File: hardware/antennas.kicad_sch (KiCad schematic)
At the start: 21 parts, among them J1001 132134

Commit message: Refine schematics
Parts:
- removed R1001, R1002, R1003, R1004, R1005, R1006, R1007, R1008: 0 Ω, perfect_footprints:R_0402_1005Metric, symbol Device:R
- added R79, R80, R81, R82, R83, R85, R86: 0 Ω, perfect_footprints:R_0402_1005Metric, symbol Device:R
- added R84: 0 Ω, perfect_footprints:R_0201_0603Metric, symbol Device:R
- renumbered AE1001 to AE1, C1001 to C52, C1002 to C53, C1003 to C54, C1004 to C55, C1005 to C56, D1001 to D15, J1001 to J20, L1001 to L3, L1002 to L4, L1003 to L5, L1004 to L6, L1005 to L7
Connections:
- net ANT: now also R79.1, R80.1
- net ANT_PCB_FILTERED: now also R82.1, R84.1
- net ANT_PCB_MATCHED: now also R84.2, R86.1
- net ANT_SEL_PCB: now also R80.2
- net ANT_SEL_SMA: now also R79.2, R81.1, R83.1
- net ANT_SMA_MATCHED: now also R83.2, R85.1
- net GND: now also R81.2, R82.2, R85.2, R86.2
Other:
- note added: "Antenna front-end"
- note added: "Antenna selection"
- note added: "Bandpass filter"
- note added: "Matching network"
- note added: "Notes"

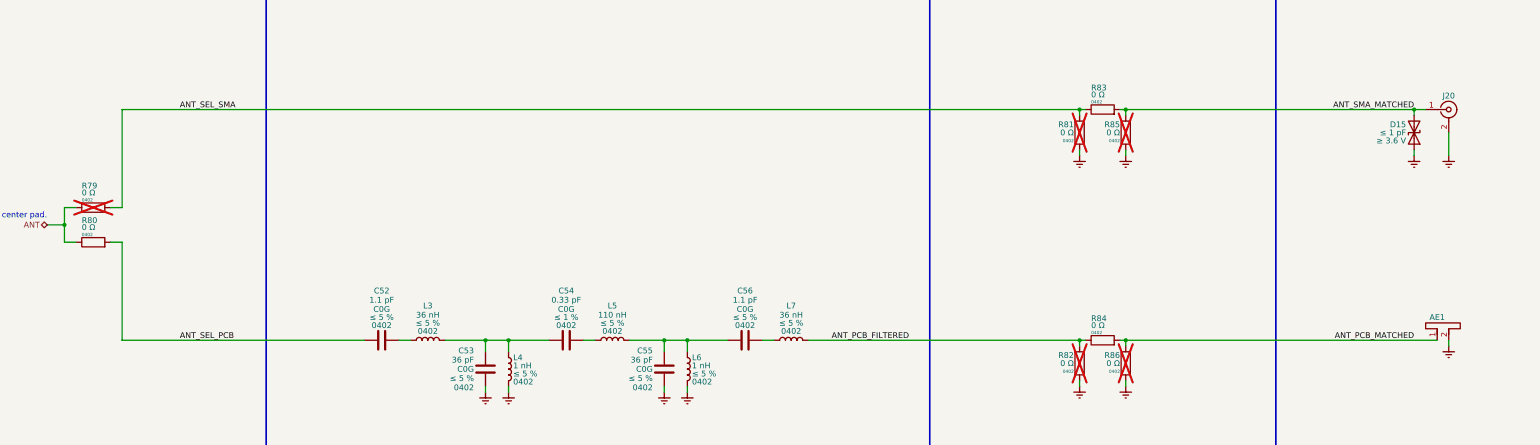
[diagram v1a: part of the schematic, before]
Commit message: HW: Redo MDM UART
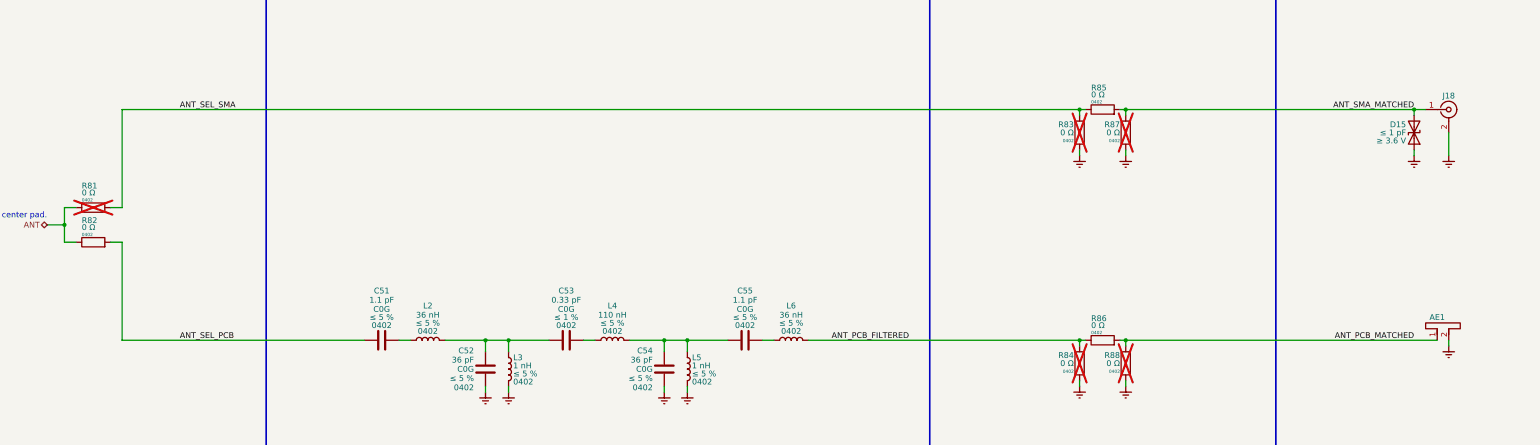
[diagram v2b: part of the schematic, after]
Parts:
- renumbered C52 to C51, C53 to C52, C54 to C53, C55 to C54, C56 to C55, J20 to J18, L3 to L2, L4 to L3, L5 to L4, L6 to L5, L7 to L6, R79 to R81, R80 to R82, R81 to R83, R82 to R84, R83 to R85, R84 to R86, R85 to R87, R86 to R88

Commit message: HW: BAT_DETn -> USB_DET
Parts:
- renumbered AE1 to AE701, C51 to C701, C52 to C702, C53 to C703, C54 to C704, C55 to C705, D15 to D701, J18 to J701, L2 to L701, L3 to L702, L4 to L703, L5 to L704, L6 to L705, R81 to R701, R82 to R702, R83 to R703, R84 to R704, R85 to R705, R86 to R706, R87 to R707, R88 to R708

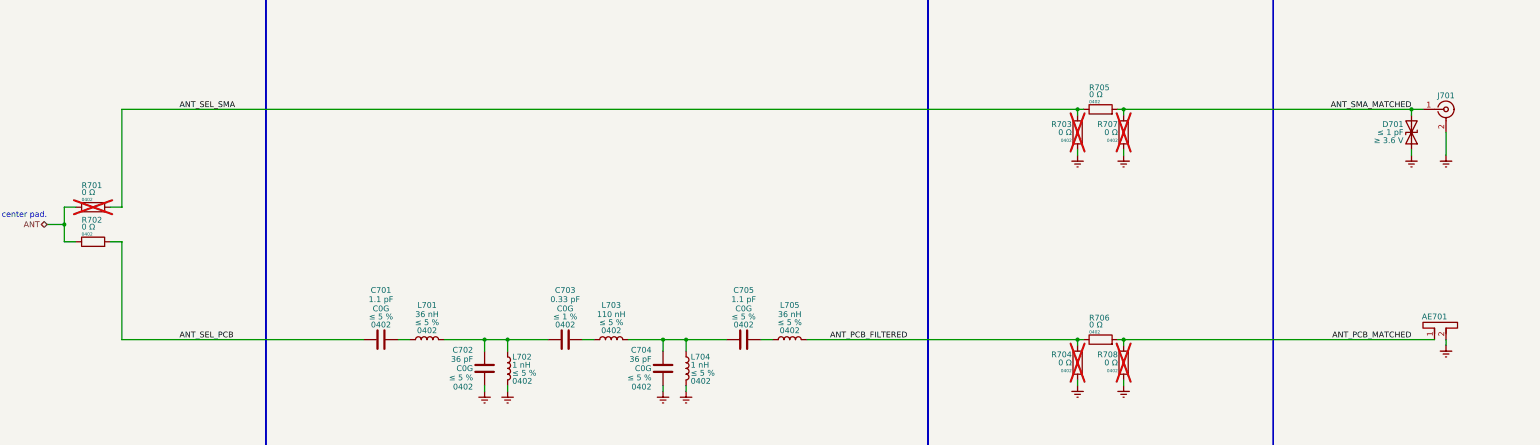
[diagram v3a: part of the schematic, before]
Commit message: HW: Move SIM to Modem
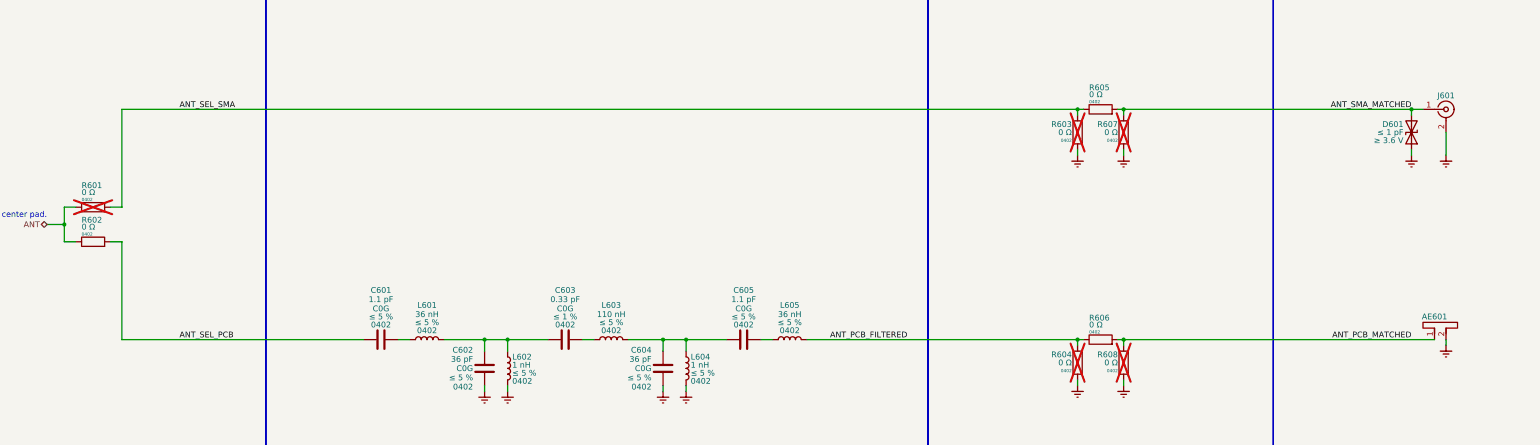
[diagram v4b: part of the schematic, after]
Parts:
- renumbered AE701 to AE601, C701 to C601, C702 to C602, C703 to C603, C704 to C604, C705 to C605, D701 to D601, J701 to J601, L701 to L601, L702 to L602, L703 to L603, L704 to L604, L705 to L605, R701 to R601, R702 to R602, R703 to R603, R704 to R604, R705 to R605, R706 to R606, R707 to R607, R708 to R608

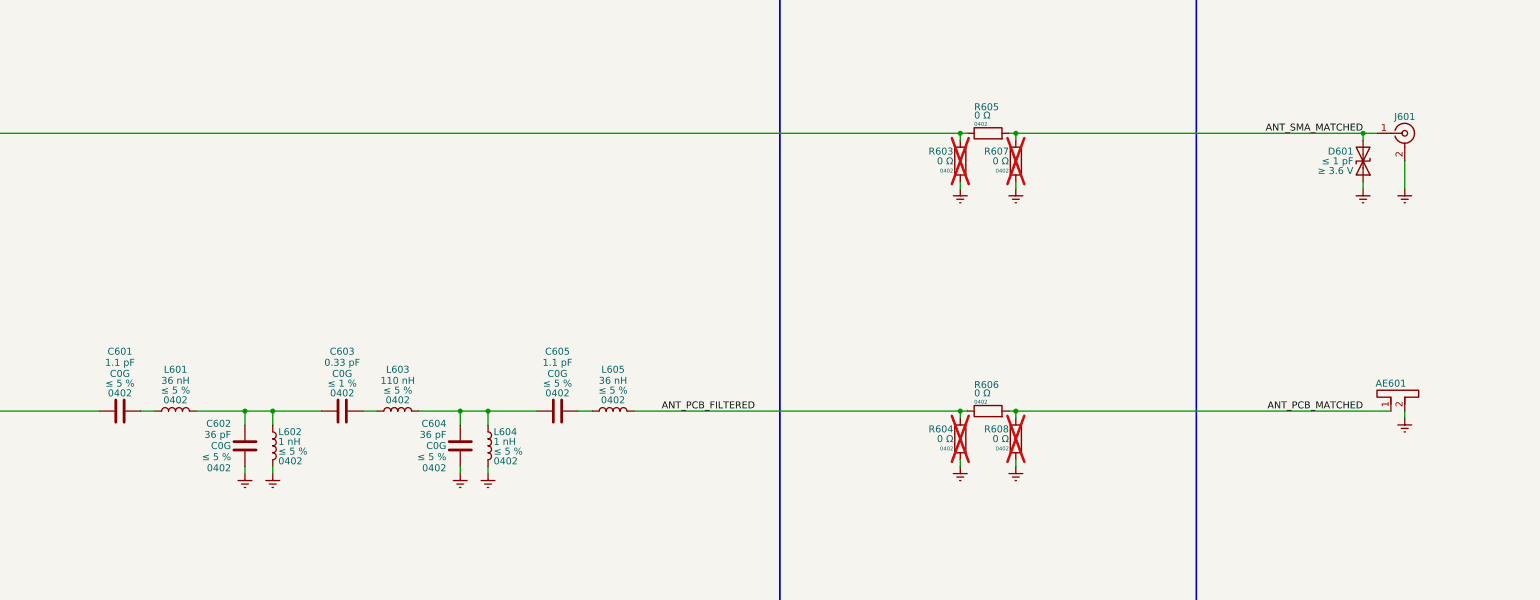
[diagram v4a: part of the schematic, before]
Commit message: HW: Refine Antennas
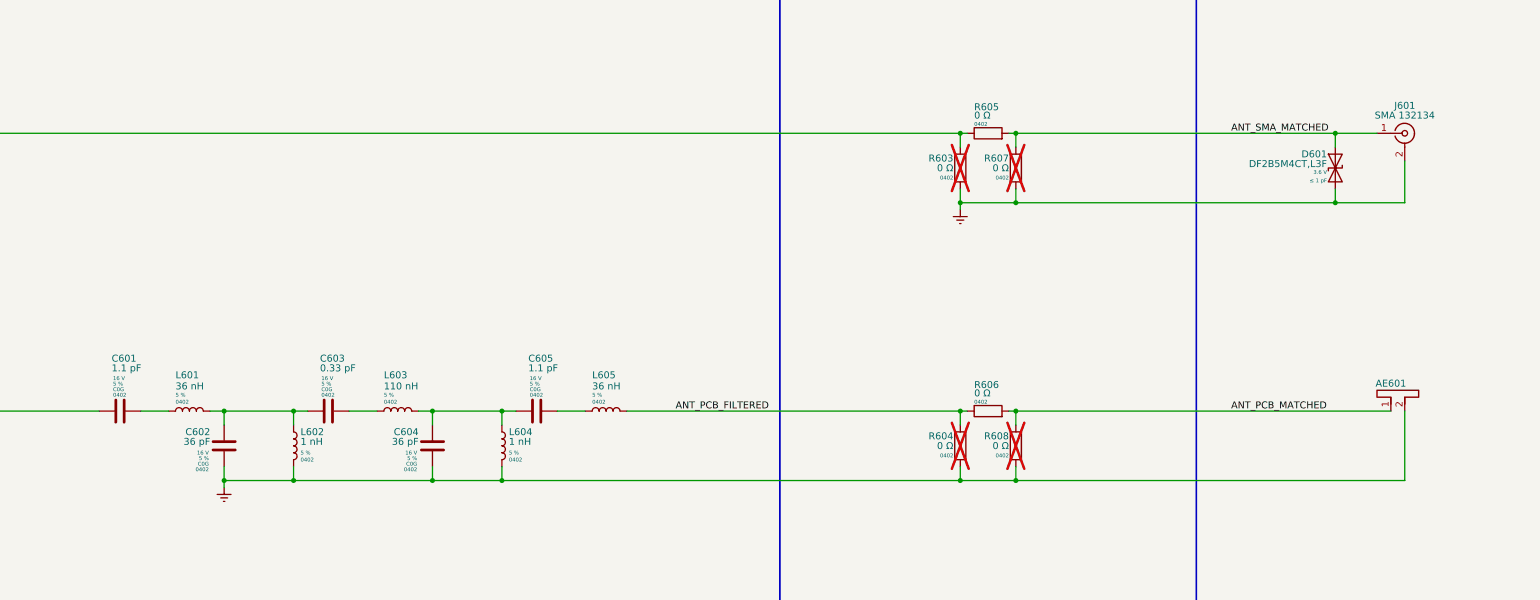
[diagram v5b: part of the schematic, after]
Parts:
- C601, C605: Class C0G -> (none); DigiKey Part Number 732-13231-1-ND -> (none); MPN 885392005006 -> (none); Manufacturer Würth Elektronik -> (none); Temperature coefficient (none) -> C0G; Tolerance ≤ 5 % -> 5 %; Voltage rating (none) -> 16 V
- C602, C604: footprint perfect_footprints:C_0402_1005Metric -> perfect_footprints:C_0201_0603Metric; Class C0G -> (none); DigiKey Part Number 490-GJM1555C1H360FB01DCT-ND -> (none); MPN GJM1555C1H360FB01D -> (none); Manufacturer Murata Electronics -> (none); Temperature coefficient (none) -> C0G; Tolerance ≤ 5 % -> 5 %; Voltage rating (none) -> 16 V
- C603: Class C0G -> (none); DigiKey Part Number 732-13226-1-ND -> (none); MPN 885392005001 -> (none); Manufacturer Würth Elektronik -> (none); Temperature coefficient (none) -> C0G; Tolerance ≤ 1 % -> 5 %; Voltage rating (none) -> 16 V
- D601: Breakdown voltage (none) -> 3.6 V; Digi-Key Part Number (none) -> DF2B5M4CTL3FCT-ND; DigiKey Part Number DF2B5M4CTL3FCT-ND -> (none); Footprint review check + -> (none); Voltage ≥ 3.6 V -> (none)
- J601: value 132134 -> SMA 132134
- L601, L605: DigiKey Part Number 732-7447650136CT-ND -> (none); MPN 7447650136 -> (none); Manufacturer Würth Elektronik -> (none); Tolerance ≤ 5 % -> 5 %
- L602, L604: DigiKey Part Number 732-2912-1-ND -> (none); MPN 744901010 -> (none); Manufacturer Würth Elektronik -> (none); Tolerance ≤ 5 % -> 5 %
- L603: DigiKey Part Number 490-12204-1-ND -> (none); MPN LQW15CAR11J00D -> (none); Manufacturer Murata Electronics -> (none); Tolerance ≤ 5 % -> 5 %
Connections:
- net ANT_PCB_FILTERED: now also L605.1; no longer L605.2
- net ANT_SMA_MATCHED: now also D601.1 (A1); no longer D601.2 (A2)
- net GND: now also C602.2, C604.2, D601.2 (A2); no longer C602.1, C604.1, D601.1 (A1)
- net at L601.1: now also C602.1, C603.1, L602.2; no longer C601.2
- net at C605.1, L604.2: now also C604.1, L603.1; no longer C604.2, L603.2
- net at C605.2: now also L605.2; no longer L605.1
- net at C603.2: now also L603.2; no longer L603.1
- new net: C601.2, L601.2
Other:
- moved on the sheet: R603, R604, R607, R608

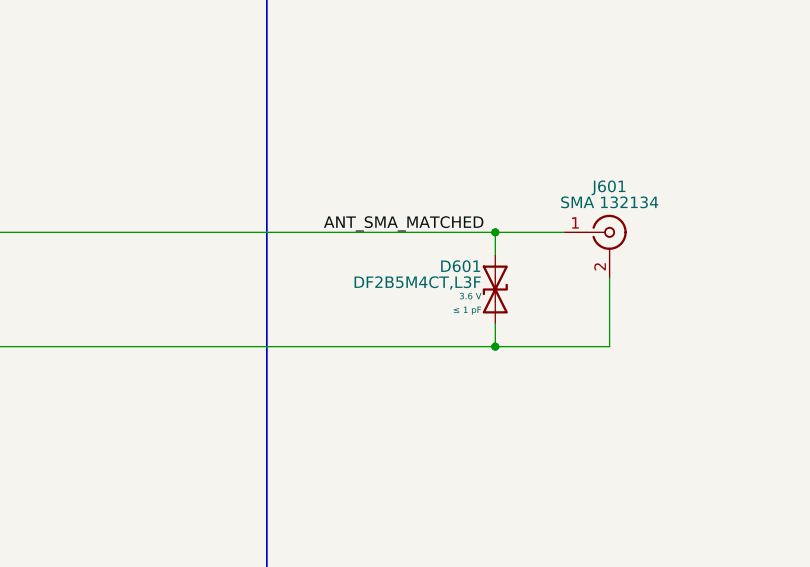
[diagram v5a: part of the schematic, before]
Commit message: HW: Set minimum passive size to 0402
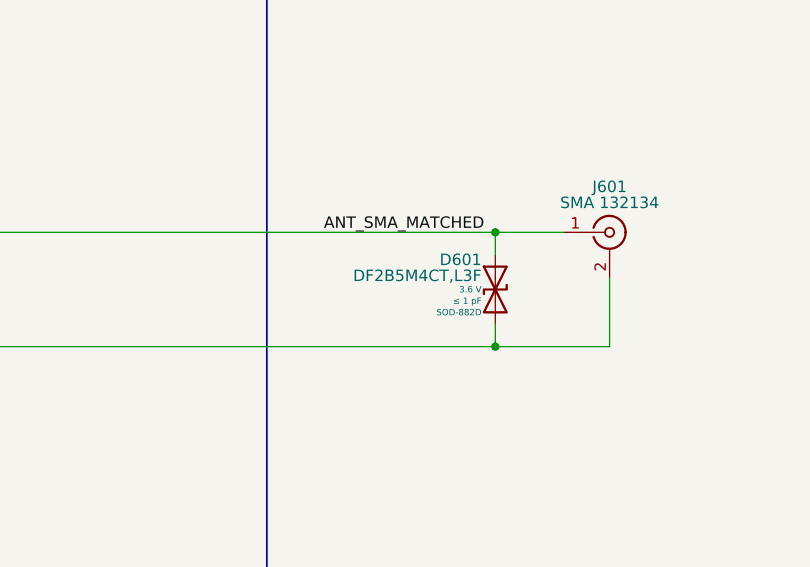
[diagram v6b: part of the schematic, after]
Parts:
- D601: Size (none) -> SOD-882D

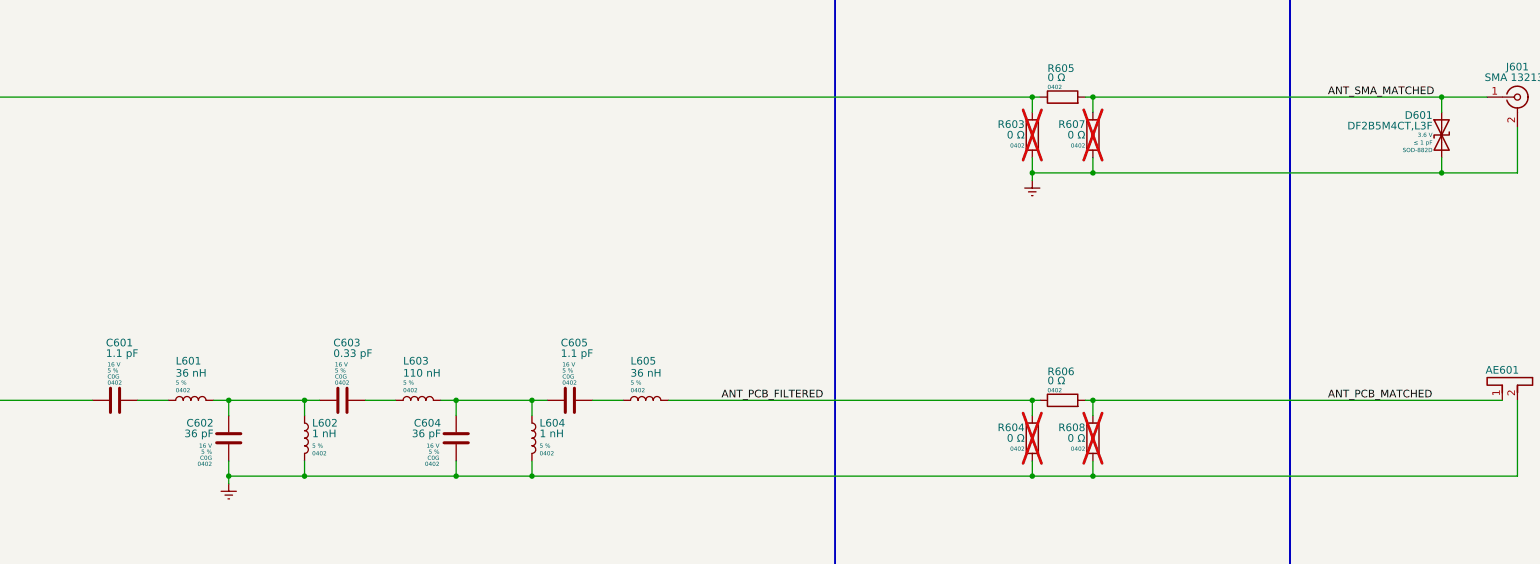
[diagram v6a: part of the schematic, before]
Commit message: HW: Fill symbol part info
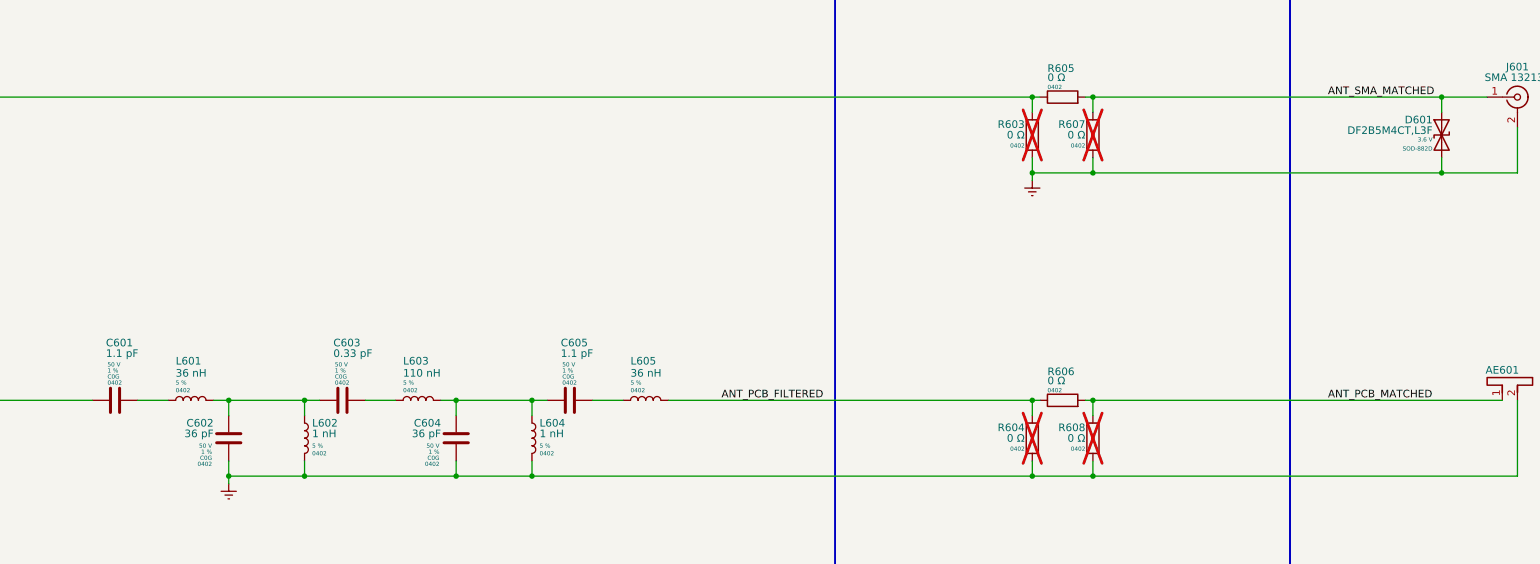
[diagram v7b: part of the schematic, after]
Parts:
- C601, C602, C603, C604, C605: Tolerance 5 % -> 1 %; Voltage rating 16 V -> 50 V
- D601: Capacitance ≤ 1 pF -> (none); Digi-Key Part Number DF2B5M4CTL3FCT-ND -> (none); MPN DF2B5M4CT,L3F -> (none); Manufacturer Toshiba Semiconductor and Storage -> (none)
- J601: DigiKey Part Number ACX1230-ND -> (none); Footprint review check + -> (none); MPN 132134 -> (none); Manufacturer Amphenol RF -> (none)
- R606: footprint perfect_footprints:R_0201_0603Metric -> perfect_footprints:R_0402_1005Metric
